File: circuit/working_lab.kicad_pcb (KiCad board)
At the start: 2 copper layers, 12 parts, among them J1 Screw_Terminal_01x02, J2 USART, J3 Conn_01x05, J4 Conn_01x03, U1 L7805, U2 PIC16F886-IP, Y1 Crystal

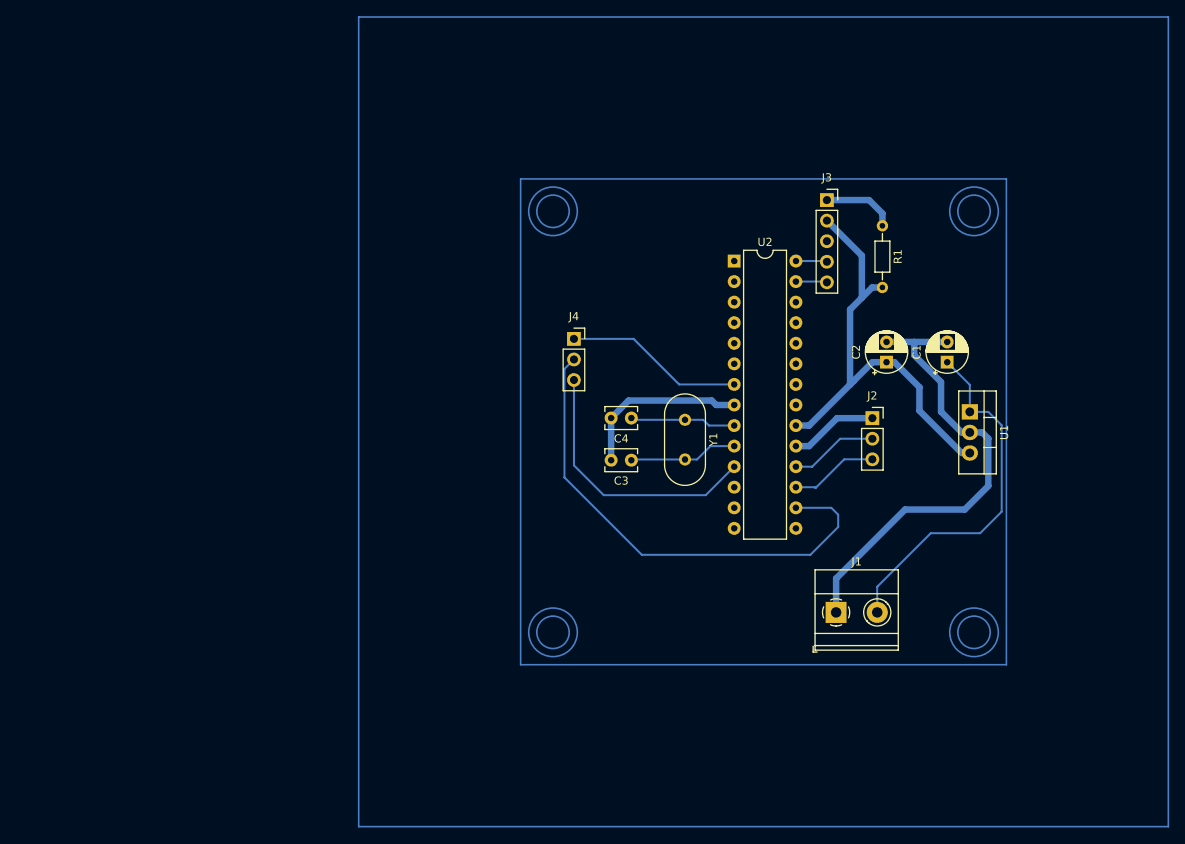
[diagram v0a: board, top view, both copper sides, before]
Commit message: I2C connection in circuit created
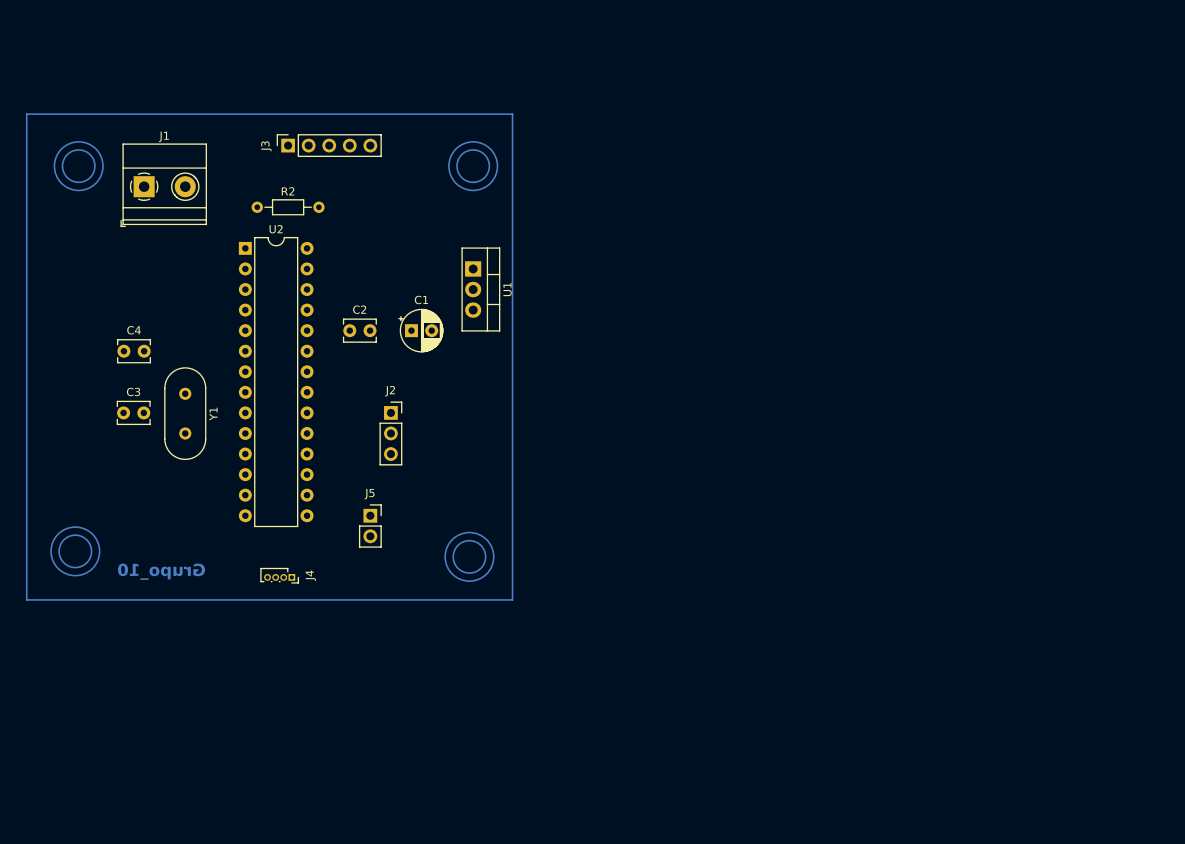
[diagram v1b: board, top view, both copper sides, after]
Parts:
- removed R1: 5k, Resistor_THT:R_Axial_DIN0204_L3.6mm_D1.6mm_P7.62mm_Horizontal
- added J5: I2C, Connector_PinSocket_2.54mm:PinSocket_1x02_P2.54mm_Vertical, F.Cu at (91.4, 101.6)
- added R2: 5K, Resistor_THT:R_Axial_DIN0204_L3.6mm_D1.6mm_P7.62mm_Horizontal, F.Cu at (77.5, 63.5)
- C2: footprint Capacitor_THT:CP_Radial_D5.0mm_P2.50mm -> Capacitor_THT:C_Disc_D3.8mm_W2.6mm_P2.50mm
- J2: value USART -> UART
- J3: value Conn_01x05 -> PIC_KIT
- J4: value Conn_01x03 -> SPI; footprint Connector_PinSocket_2.54mm:PinSocket_1x03_P2.54mm_Vertical -> Connector_PinSocket_1.00mm:PinSocket_1x04_P1.00mm_Vertical
- Y1: value Crystal -> 2MHz
- moved J1 100.3 mm to (63.5, 61.0)
- moved J3 66.9 mm to (81.3, 55.9), turned to 90 degrees
- moved C2 66.4 mm to (88.9, 78.7), turned to 0 degrees
- moved C1 66.3 mm to (96.5, 78.7), turned to 0 degrees
- moved U1 63.8 mm to (104.1, 71.1)
- moved C4 63.2 mm to (61.0, 81.3), turned to 0 degrees
- moved C3 63.0 mm to (61.0, 88.9), turned to 0 degrees
- moved Y1 61.8 mm to (68.6, 86.5)
- moved U2 60.4 mm to (76.0, 68.6)
- moved J2 59.5 mm to (94.0, 88.9)
- moved J4 45.6 mm to (81.7, 109.2), turned to -90 degrees
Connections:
- C1 pad 1: +12V -> GND
- C1 pad 2: GND -> +12V
- C2 pad 1: +5V -> GND
- C2 pad 2: GND -> VDD
- J3 pad 2: +5V -> VDD
- J3 pad 4: icsp_dat -> ICSPCLK
- J3 pad 5: icsp_clk -> ICSPDAT
- J4 pad 1: Net-(J4-Pin_1) -> unconnected-(J4-Pin_1-Pad1)
- J4 pad 2: dataOUT -> SS
- J4 pad 3: clk -> dataOUT
- U1 pad 3: +5V -> VDD
- U2 pad 14: unconnected-(U2-RC3/SCK/SCL-Pad14) -> Net-(J5-Pin_2)
- U2 pad 15: unconnected-(U2-RC4/SDI/SDA-Pad15) -> Net-(J5-Pin_1)
- U2 pad 20: +5V -> VDD
- U2 pad 27: icsp_clk -> ICSPCLK
- U2 pad 28: icsp_dat -> ICSPDAT
- U2 pad 7: Net-(J4-Pin_1) -> SS
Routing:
- net GND: track 90.7 -> 0.00 mm
- net dataOUT: track 61.4 -> 0.00 mm
- net +5V: track 56.8 -> 0.00 mm
- net +12V: track 45.0 -> 0.00 mm
- net clk: track 33.3 -> 0.00 mm
- net Net-(J4-Pin_1): track 22.1 -> 0.00 mm
- net Net-(U2-CLKOUT/OSC2/RA6): track 13.4 -> 0.00 mm
- net Net-(U2-CLKIN/OSC1/RA7): track 13.1 -> 0.00 mm
- net tx: track 10.9 -> 0.00 mm
- net rx: track 10.9 -> 0.00 mm
- net mclr: track 9.07 -> 0.00 mm
- net icsp_dat: track 3.87 -> 0.00 mm
- net icsp_clk: track 3.87 -> 0.00 mm
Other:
- board text added: "Grupo_10"

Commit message: connections update
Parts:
- moved C1 34.3 mm to (64.0, 67.8), turned to 90 degrees
- moved U1 31.3 mm to (75.3, 58.9), turned to 0 degrees
- moved J3 24.9 mm to (91.4, 78.6), turned to 180 degrees
- moved R2 21.6 mm to (98.3, 69.1), turned to -90 degrees
- moved C2 18.3 mm to (104.6, 69.5), turned to -90 degrees
- moved J4 17.7 mm to (65.6, 101.8), turned to 180 degrees
- moved J1 11.8 mm to (55.0, 69.1), turned to 90 degrees
- moved J5 11.4 mm to (80.8, 105.6), turned to -90 degrees
- moved C4 7.49 mm to (64.8, 87.8), turned to 180 degrees
- moved C3 5.28 mm to (64.8, 92.6), turned to 180 degrees
- moved J2 2.79 mm to (92.8, 91.4)
- moved Y1 1.56 mm to (69.6, 87.7)
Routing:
- net GND: track 0.00 -> 239.6 mm
- net VDD: track 0.00 -> 84.6 mm
- net mclr: track 0.00 -> 42.6 mm
- net SS: track 0.00 -> 38.2 mm
- net dataOUT: track 0.00 -> 35.0 mm
- net +12V: track 0.00 -> 23.5 mm
- net clk: track 0.00 -> 12.4 mm
- net Net-(U2-CLKOUT/OSC2/RA6): track 0.00 -> 11.8 mm
- net Net-(U2-CLKIN/OSC1/RA7): track 0.00 -> 11.7 mm
- net tx: track 0.00 -> 9.22 mm
- net rx: track 0.00 -> 9.22 mm
- net ICSPCLK: track 0.00 -> 7.87 mm
- net ICSPDAT: track 0.00 -> 7.87 mm
- net Net-(J5-Pin_1): track 0.00 -> 5.74 mm
- net Net-(J5-Pin_2): track 0.00 -> 4.88 mm

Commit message: circuit update
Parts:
- J4: footprint Connector_PinSocket_1.00mm:PinSocket_1x04_P1.00mm_Vertical -> Connector_PinSocket_2.54mm:PinSocket_1x02_P2.54mm_Vertical
- moved J4 0.47 mm to (66.0, 101.6), turned to 90 degrees
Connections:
- J4 pad 1: unconnected-(J4-Pin_1-Pad1) -> dataOUT
- J4 pad 2: SS -> clk
- U2 pad 7: SS -> unconnected-(U2-~{SS}/C2OUT/AN4/RA5-Pad7)
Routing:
- net GND: track 239.6 -> 288.5 mm
- net SS: track 38.2 -> 0.00 mm
- net dataOUT: track 35.0 -> 23.8 mm
- net mclr: track 42.6 -> 39.7 mm
- net clk: track 12.4 -> 10.7 mm
- net unconnected-(U2-~{SS}/C2OUT/AN4/RA5-Pad7): track 0.00 -> 0.82 mm

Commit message: circuit completed
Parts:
- added J6: PWM, Connector_PinSocket_2.54mm:PinSocket_1x01_P2.54mm_Vertical, F.Cu at (68.6, 101.6)
- added J7: Analogic, Connector_PinSocket_2.54mm:PinSocket_1x03_P2.54mm_Vertical, F.Cu at (88.9, 81.3)
- moved R2 31.6 mm to (68.6, 58.4), turned to 0 degrees
- moved U1 30.2 mm to (101.6, 73.7), turned to 90 degrees
- moved J3 23.3 mm to (73.7, 63.5), turned to 90 degrees
- moved C2 15.4 mm to (94.0, 58.4), turned to 90 degrees
- moved Y1 8.70 mm to (61.0, 89.1)
- moved C3 7.48 mm to (61.0, 99.1)
- moved J2 6.27 mm to (96.5, 96.5)
- moved C4 5.48 mm to (61.0, 83.8)
- moved J4 5.08 mm to (66.0, 96.5), turned to 180 degrees
- moved C1 4.65 mm to (68.6, 68.6)
- moved U2 2.34 mm to (73.7, 68.6)
- moved J5 2.30 mm to (78.7, 106.7)
- moved J1 2.22 mm to (55.9, 71.1)
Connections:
- U2 pad 13: unconnected-(U2-RC2/P1A/CCP1-Pad13) -> Net-(J6-Pin_1)
- U2 pad 21: unconnected-(U2-INT/AN12/RB0-Pad21) -> Net-(J7-Pin_1)
- U2 pad 22: unconnected-(U2-P1C/AN10/RB1-Pad22) -> Net-(J7-Pin_2)
- U2 pad 23: unconnected-(U2-P1B/AN8/RB2-Pad23) -> Net-(J7-Pin_3)
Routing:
- net GND: track 288.5 -> 202.6 mm
- net +12V: track 23.5 -> 81.6 mm
- net mclr: track 39.7 -> 12.3 mm
- net VDD: track 84.6 -> 68.5 mm
- net dataOUT: track 23.8 -> 36.1 mm
- net Net-(J7-Pin_3): track 0.00 -> 9.72 mm
- net Net-(J7-Pin_2): track 0.00 -> 9.72 mm
- net Net-(J7-Pin_1): track 0.00 -> 9.72 mm
- net tx: track 9.22 -> 17.3 mm
- net rx: track 9.22 -> 17.3 mm
- net Net-(U2-CLKOUT/OSC2/RA6): track 11.8 -> 18.8 mm
- net Net-(U2-CLKIN/OSC1/RA7): track 11.7 -> 18.0 mm
- net Net-(J6-Pin_1): track 0.00 -> 6.13 mm
- net clk: track 10.7 -> 7.62 mm
- net ICSPCLK: track 7.87 -> 10.4 mm
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
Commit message: first version of the circuit and starting code
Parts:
- moved C2 7.62 mm to (86.4, 58.4)
- moved J7 3.59 mm to (86.4, 83.8)
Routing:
- net Net-(J7-Pin_2): track 9.72 -> 6.13 mm
- net Net-(J7-Pin_3): track 9.72 -> 6.13 mm
- net Net-(J7-Pin_1): track 9.72 -> 6.13 mm
- net dataOUT: track 36.1 -> 38.9 mm
- net VDD: track 68.5 -> 66.4 mm
